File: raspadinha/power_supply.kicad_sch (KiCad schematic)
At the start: 2 parts, among them J1 ATX-24

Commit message: feat: usando o mosfet IRFZ44N feat: switch de on/off na fonte de alimentação
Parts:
- added SW2: SW_SPST, symbol Switch:SW_SPST
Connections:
- net at R1.1: now also SW2.2 (B); no longer J1.16 (PS_ON#)
- new net: J1.16 (PS_ON#), SW2.1 (A)
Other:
- moved on the sheet: R1
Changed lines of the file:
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@@
+	(wire
+		(pts
+			(xy 100.33 101.6) (xy 100.33 105.41)
+		)
+		(stroke
+			(width 0)
+			(type default)
+		)
+	)
 	(wire
 		(pts
@@
 	(wire
 		(pts
-			(xy 109.22 90.17) (xy 105.41 90.17)
-		)
-		(stroke
-			(width 0)
-			(type default)
-		)
-	)
-	(wire
-		(pts
 			(xy 121.92 115.57) (xy 121.92 118.11)
 		)
@@
 	(wire
 		(pts
+			(xy 100.33 90.17) (xy 100.33 91.44)
+		)
+		(stroke
+			(width 0)
+			(type default)
+		)
+	)
+	(wire
+		(pts
 			(xy 134.62 102.87) (xy 139.7 102.87)
 		)
@@
 	(wire
 		(pts
-			(xy 105.41 90.17) (xy 105.41 91.44)
-		)
-		(stroke
-			(width 0)
-			(type default)
-		)
-	)
-	(wire
-		(pts
 			(xy 134.62 95.25) (xy 139.7 95.25)
 		)
@@
 	(wire
 		(pts
-			(xy 105.41 99.06) (xy 105.41 101.6)
+			(xy 100.33 113.03) (xy 100.33 118.11)
+		)
+		(stroke
+			(width 0)
+			(type default)
+		)
+	)
+	(wire
+		(pts
+			(xy 100.33 90.17) (xy 109.22 90.17)
 		)
 		(stroke
@@
 	(hierarchical_label "GND"
 		(shape output)
-		(at 105.41 101.6 270)
+		(at 100.33 118.11 270)
 		(effects
 			(font
@@
 	(symbol
 		(lib_id "Device:R")
-		(at 105.41 95.25 0)
+		(at 100.33 109.22 0)
 		(unit 1)
 		(exclude_from_sim no)
@@
 		(fields_autoplaced yes)
 		(property "Reference" "R1"
-			(at 107.95 93.9799 0)
+			(at 102.87 107.9499 0)
 			(effects
 				(font
@@
 		)
 		(property "Value" "0R"
-			(at 107.95 96.5199 0)
+			(at 102.87 110.4899 0)
 			(effects
 				(font
@@
 		)
 		(property "Footprint" ""
-			(at 103.632 95.25 90)
+			(at 98.552 109.22 90)
 			(effects
 				(font
@@
 		)
 		(property "Datasheet" "~"
-			(at 105.41 95.25 0)
+			(at 100.33 109.22 0)
 			(effects
 				(font
@@
 		)
 		(property "Description" "Resistor"
-			(at 105.41 95.25 0)
+			(at 100.33 109.22 0)
 			(effects
 				(font
@@
 					(unit 1)
 				)
+			)
+		)
+	)
+	(symbol
+		(lib_id "Switch:SW_SPST")
+		(at 100.33 96.52 270)
+		(unit 1)
+		(exclude_from_sim no)
+		(in_bom yes)
+		(on_board yes)
+		(dnp no)
+		(fields_autoplaced yes)
+		(property "Reference" "SW2"
+			(at 102.87 95.2499 90)
+			(effects
+				(font
+					(size 1.27 1.27)
+				)
+				(justify left)
+			)
+		)
+		(property "Value" "SW_SPST"
+			(at 102.87 97.7899 90)
+			(effects
+				(font
+					(size 1.27 1.27)
+				)
+				(justify left)
+			)
+		)
+		(property "Footprint" ""
+			(at 100.33 96.52 0)
+			(effects
+				(font
+					(size 1.27 1.27)
+				)
+				(hide yes)
+			)
+		)
+		(property "Datasheet" "~"
+			(at 100.33 96.52 0)
+			(effects
+				(font
+					(size 1.27 1.27)
+				)
+				(hide yes)
+			)
+		)
+		(property "Description" "Single Pole Single Throw (SPST) switch"
+			(at 100.33 96.52 0)
+			(effects
+				(font
+					(size 1.27 1.27)
+				)
+				(hide yes)
+			)
+		)
+		(pin "2"
+		)
+		(pin "1"
+		)
+		(instances
+			(project ""
+				(path "/0ce4bf39-76b0-428c-8682-47e2500753cc/a0b53ea5-873b-403f-a5fc-d02695d9fbc8"
+					(reference "SW2")
+					(unit 1)
+				)

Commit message: feat: Os Footprint foram todos atribuidos fix: A placa da Esp32 foi trocada pela que temos disponível
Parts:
- J1: footprint (none) -> Connector_PinHeader_2.54mm:PinHeader_2x12_P2.54mm_Vertical
- SW2: footprint (none) -> Button_Switch_THT:SW_DIP_SPSTx01_Slide_6.7x4.1mm_W7.62mm_P2.54mm_LowProfile
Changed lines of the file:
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@@
 		(title "Geladinho, Power Supply")
 		(date "2025-11-20")
-		(rev "v1.0.0")
+		(rev "v1.1.0")
 		(company "Universidade Federal Do Ceará")
 	)
@@
 		(exclude_from_sim no)
 		(in_bom yes)
-		(on_board yes)
+		(on_board no)
 		(dnp no)
 		(fields_autoplaced yes)
@@
 			)
 		)
-		(property "Footprint" ""
+		(property "Footprint" "Button_Switch_THT:SW_DIP_SPSTx01_Slide_6.7x4.1mm_W7.62mm_P2.54mm_LowProfile"
 			(at 100.33 96.52 0)
 			(effects
@@
 			)
 		)
-		(property "Footprint" ""
+		(property "Footprint" "Connector_PinHeader_2.54mm:PinHeader_2x12_P2.54mm_Vertical"
 			(at 121.92 102.87 0)
 			(effects

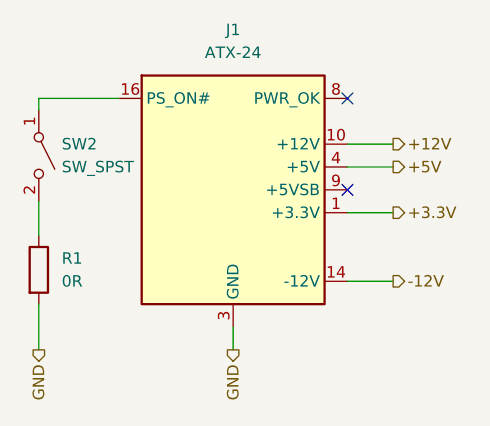
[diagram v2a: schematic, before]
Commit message: feat: Refatoração da alimentação da placa feat: Renomeação do número dos componentes
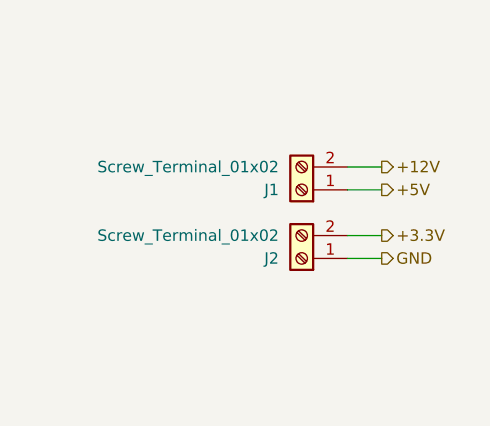
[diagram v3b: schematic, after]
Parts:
- removed J1: ATX-24, Connector_PinHeader_2.54mm:PinHeader_2x12_P2.54mm_Vertical, symbol Connector:ATX-24
- removed R1: 0R, symbol Device:R
- removed SW2: SW_SPST, Button_Switch_THT:SW_DIP_SPSTx01_Slide_6.7x4.1mm_W7.62mm_P2.54mm_LowProfile, symbol Switch:SW_SPST
- added J1, J2: Screw_Terminal_01x02, TerminalBlock_Phoenix:TerminalBlock_Phoenix_PT-1,5-2-3.5-H_1x02_P3.50mm_Horizontal, symbol Connector:Screw_Terminal_01x02
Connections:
- net +12V: now also J1.2 (Pin_2)
- net +3.3V: now also J2.2 (Pin_2)
- net +5V: now also J1.1 (Pin_1)
- net GND: now also J2.1 (Pin_1)
- no-connect marks 2 -> 0
